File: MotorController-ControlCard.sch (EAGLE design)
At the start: 38 parts, among them J1 SL07-HORIZ, Q7 MOSFET-PCHANNEL, Q8 MOSFET-PCHANNEL, U1 TMS320F28069MPZT, U3 TMS320F28069MPZT

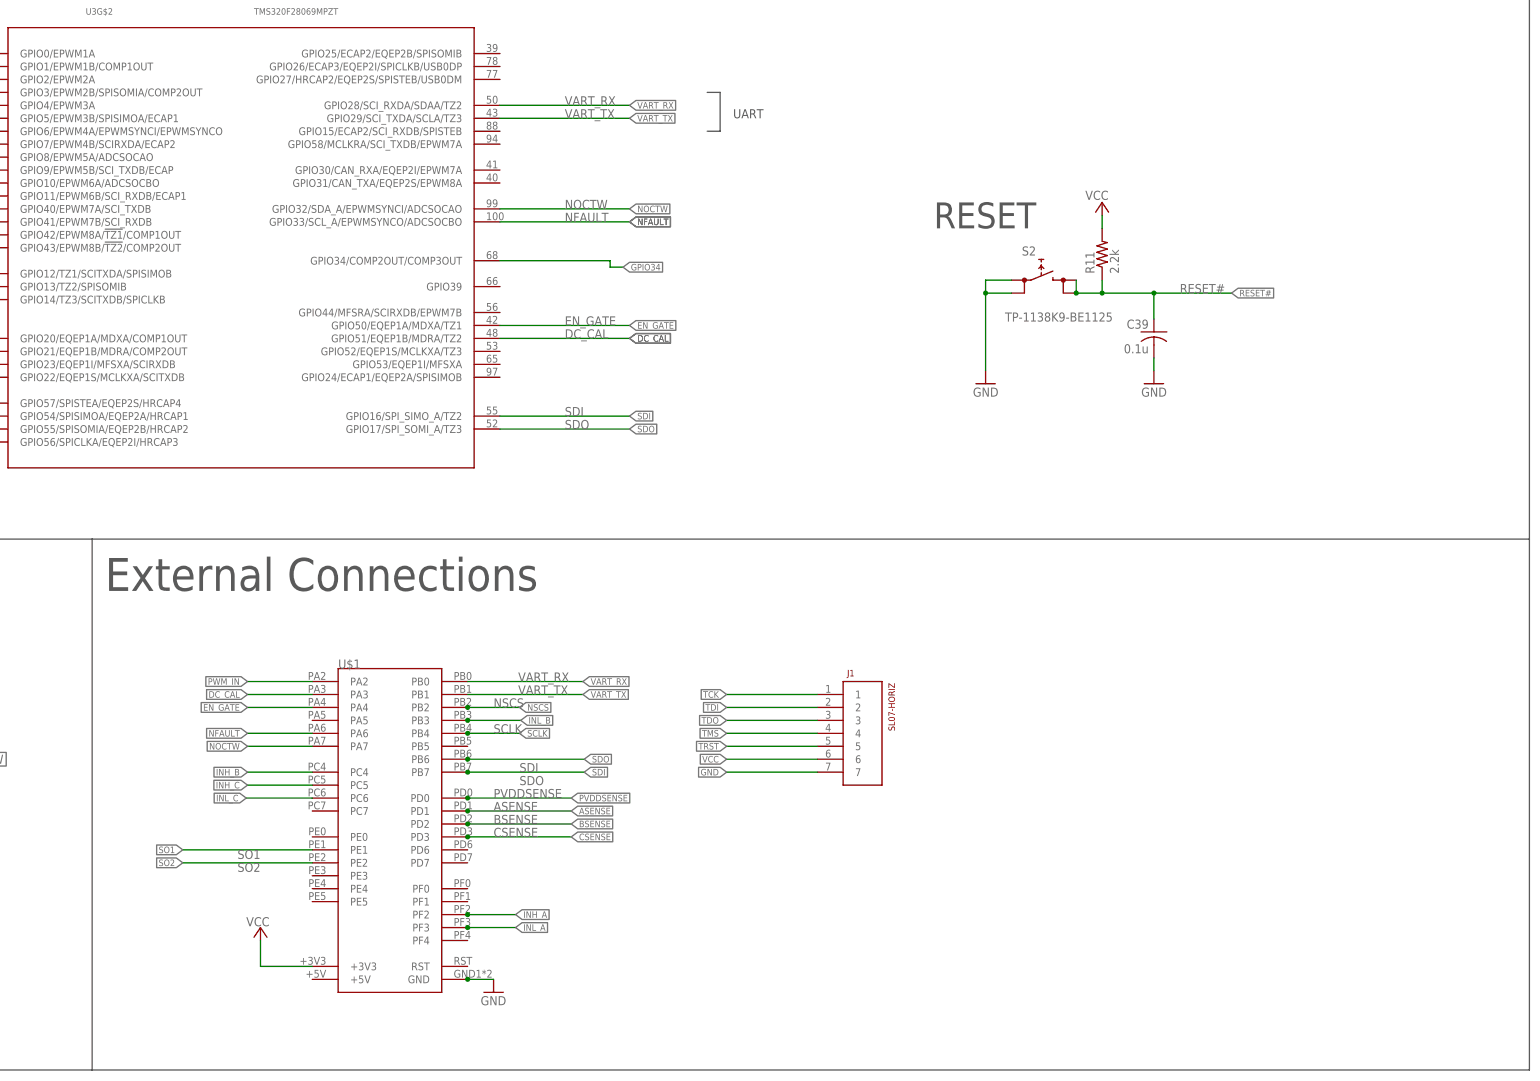
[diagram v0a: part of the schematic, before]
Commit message: Added SL connectors & MAX232, added Andrew's JTAG connector
Added SL connectors from gimbal power board and added connections to BOOSTXL header / MAX232. Same implementation as gimbal power board.
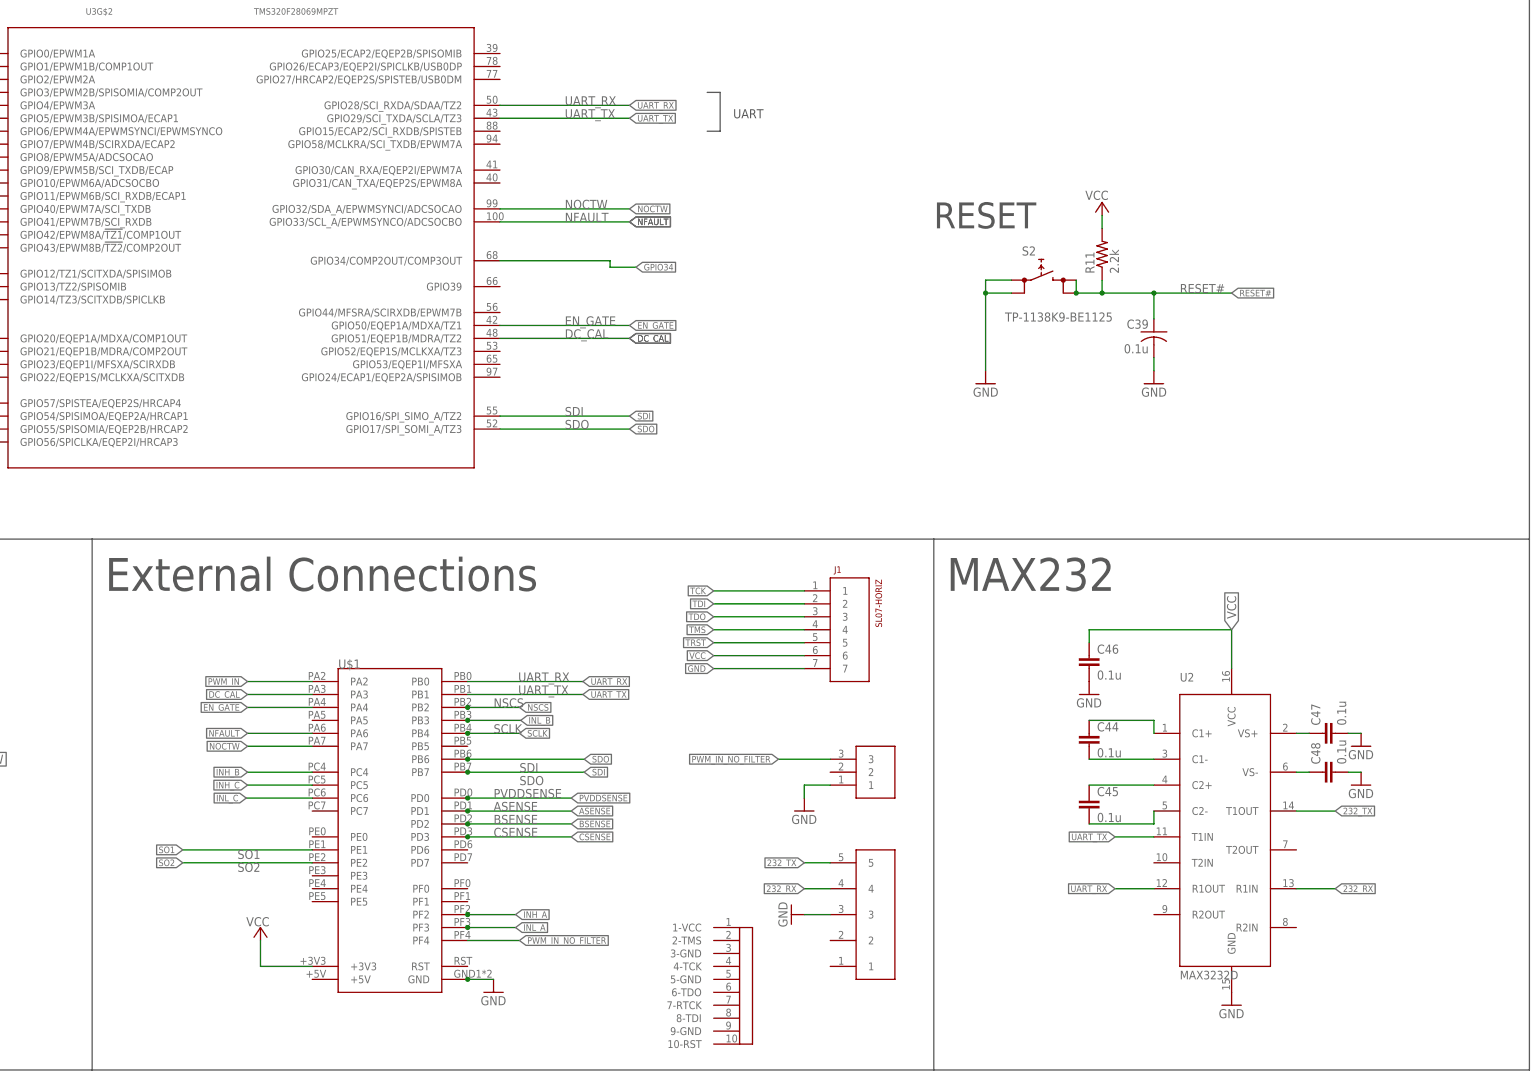
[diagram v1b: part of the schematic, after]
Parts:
- added C44, C45, C46, C47, C48: 0.1u, SparkFun-Passives:CAP0805
- added J2: SL03THROUGH_HOLE, MRDT-Connectors:SL03THROUGH_HOLE
- added U$2: IDC_BOX_HEADER_2X5_1.27MM, MRDT-Connectors:IDC_BOX_HEADER_2X5_1.27MM
- added U$4: 5PIN, Molex-SL:5PIN
- added U2: MAX3232D, MRDT-ICs:MAX3232D
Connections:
- removed net VART_RX: U$1.PB0, U3G$2.GPIO28/SCI_RXDA/SDAA/TZ2
- removed net VART_TX: U$1.PB1, U3G$2.GPIO29/SCI_TXDA/SCLA/TZ3
- new net 232_RX: U$4.4, U2.R1IN
- new net 232_TX: U$4.5, U2.T1OUT
- new net N$40: C44.1, U2.C1+
- new net N$42: C44.2, U2.C1-
- new net N$43: C45.1, U2.C2+
- new net N$44: C45.2, U2.C2-
- new net N$45: C48.1, U2.VS-
- new net N$46: C47.1, U2.VS+
- new net PWM_IN_NO_FILTER: J2.3, U$1.PF4
- new net UART_RX: U$1.PB0, U2.R1OUT, U3G$2.GPIO28/SCI_RXDA/SDAA/TZ2
- new net UART_TX: U$1.PB1, U2.T1IN, U3G$2.GPIO29/SCI_TXDA/SCLA/TZ3
- net GND: now also C46.2, C47.2, C48.2, J2.1, U$4.3, U2.GND
- net VCC: now also C46.1, U2.VCC
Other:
- note added: "MAX232"
- moved on the sheet: J1

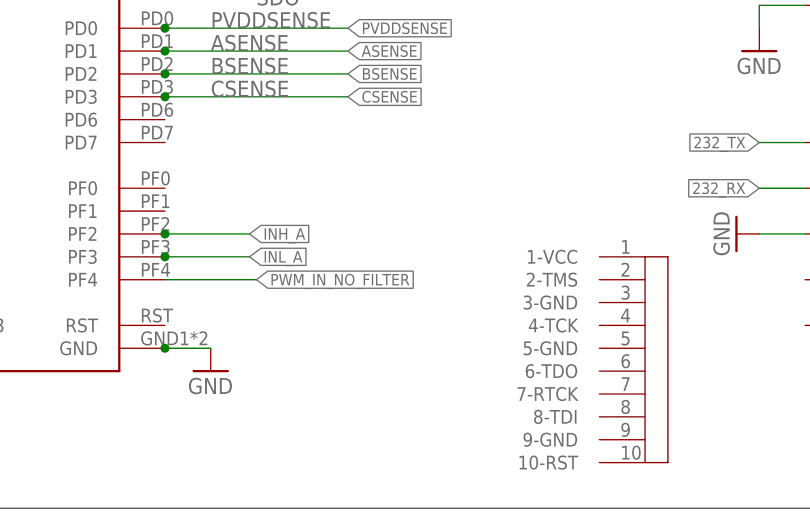
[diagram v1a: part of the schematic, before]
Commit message: Added connections to Andrew's JTAG connector
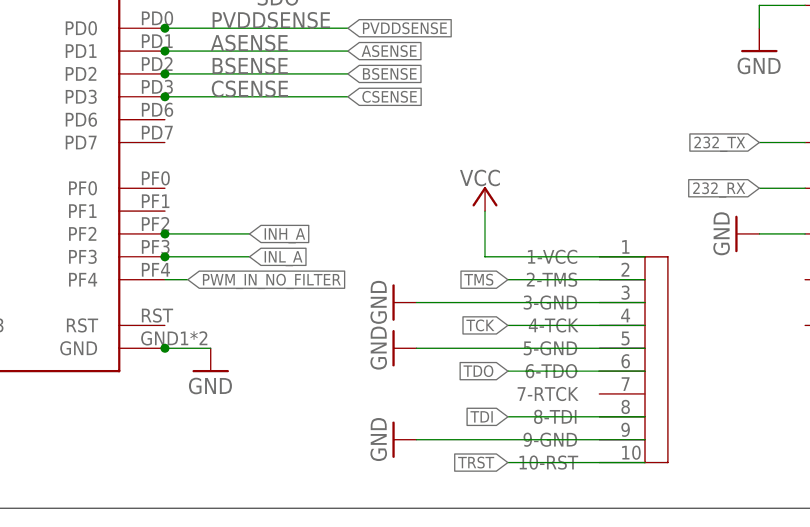
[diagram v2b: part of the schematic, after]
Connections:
- net +3V3: now also U$2.1-VCC
- net GND: now also U$2.3-GND, U$2.5-GND, U$2.9-GND
- net TCK: now also U$2.4-TCK
- net TDI: now also U$2.8-TDI
- net TDO: now also U$2.6-TDO
- net TMS: now also U$2.2-TMS
- net TRST: now also U$2.10-RST
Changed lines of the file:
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@@
 <part name="GND46" library="SparkFun-Aesthetics" deviceset="GND" device=""/>
 <part name="U$2" library="MRDT-Connectors" deviceset="IDC_BOX_HEADER_2X5_1.27MM" device=""/>
+<part name="VCC2" library="supply1" deviceset="+3V3" device="" value="VCC"/>
+<part name="GND2" library="SparkFun-Aesthetics" deviceset="GND" device=""/>
+<part name="GND3" library="SparkFun-Aesthetics" deviceset="GND" device=""/>
+<part name="GND4" library="SparkFun-Aesthetics" deviceset="GND" device=""/>
 </parts>
 <sheets>
@@
 <instance part="GND46" gate="1" x="251.46" y="-73.66"/>
 <instance part="U$2" gate="1" x="129.54" y="-124.46"/>
+<instance part="VCC2" gate="G$1" x="111.76" y="-93.98" smashed="yes">
+<attribute name="VALUE" x="108.966" y="-93.726" size="1.778" layer="96"/>
+</instance>
+<instance part="GND2" gate="1" x="101.6" y="-106.68" rot="R270"/>
+<instance part="GND3" gate="1" x="101.6" y="-111.76" rot="R270"/>
+<instance part="GND4" gate="1" x="101.6" y="-121.92" rot="R270"/>
 </instances>
 <busses>
@@
 <wire x1="251.46" y1="-71.12" x2="248.92" y2="-71.12" width="0.1524" layer="91"/>
 </segment>
+<segment>
+<pinref part="U$2" gate="1" pin="3-GND"/>
+<wire x1="129.54" y1="-106.68" x2="104.14" y2="-106.68" width="0.1524" layer="91"/>
+<pinref part="GND2" gate="1" pin="GND"/>
+</segment>
+<segment>
+<pinref part="U$2" gate="1" pin="5-GND"/>
+<wire x1="129.54" y1="-111.76" x2="104.14" y2="-111.76" width="0.1524" layer="91"/>
+<pinref part="GND3" gate="1" pin="GND"/>
+</segment>
+<segment>
+<pinref part="U$2" gate="1" pin="9-GND"/>
+<wire x1="129.54" y1="-121.92" x2="104.14" y2="-121.92" width="0.1524" layer="91"/>
+<pinref part="GND4" gate="1" pin="GND"/>
+</segment>
 </net>
 <net name="NOCTW" class="0">
@@
 <wire x1="35.56" y1="-109.22" x2="45.72" y2="-109.22" width="0.1524" layer="91"/>
 </segment>
+<segment>
+<pinref part="VCC2" gate="G$1" pin="+3V3"/>
+<wire x1="111.76" y1="-96.52" x2="111.76" y2="-101.6" width="0.1524" layer="91"/>
+<pinref part="U$2" gate="1" pin="1-VCC"/>
+<wire x1="111.76" y1="-101.6" x2="129.54" y2="-101.6" width="0.1524" layer="91"/>
+</segment>
 </net>
 <net name="TCK" class="0">
@@
 <label x="124.46" y="-35.56" size="1.27" layer="95" rot="R180" xref="yes"/>
 </segment>
+<segment>
+<pinref part="U$2" gate="1" pin="4-TCK"/>
+<wire x1="129.54" y1="-109.22" x2="114.3" y2="-109.22" width="0.1524" layer="91"/>
+<label x="114.3" y="-109.22" size="1.27" layer="95" rot="R180" xref="yes"/>
+</segment>
 </net>
 <net name="TDI" class="0">
@@
 <wire x1="142.24" y1="-38.1" x2="124.46" y2="-38.1" width="0.1524" layer="91"/>
 <label x="124.46" y="-38.1" size="1.27" layer="95" rot="R180" xref="yes"/>
+</segment>
+<segment>
+<pinref part="U$2" gate="1" pin="8-TDI"/>
+<wire x1="129.54" y1="-119.38" x2="114.3" y2="-119.38" width="0.1524" layer="91"/>
+<label x="114.3" y="-119.38" size="1.27" layer="95" rot="R180" xref="yes"/>
 </segment>
 </net>
@@
 <pinref part="U1" gate="G$1" pin="TDO/GPIO37"/>
 </segment>
+<segment>
+<pinref part="U$2" gate="1" pin="6-TDO"/>
+<wire x1="129.54" y1="-114.3" x2="114.3" y2="-114.3" width="0.1524" layer="91"/>
+<label x="114.3" y="-114.3" size="1.27" layer="95" rot="R180" xref="yes"/>
+</segment>
 </net>
 <net name="TMS" class="0">
@@
 <wire x1="142.24" y1="-43.18" x2="124.46" y2="-43.18" width="0.1524" layer="91"/>
 <label x="124.46" y="-43.18" size="1.27" layer="95" rot="R180" xref="yes"/>
+</segment>
+<segment>
+<pinref part="U$2" gate="1" pin="2-TMS"/>
+<wire x1="129.54" y1="-104.14" x2="114.3" y2="-104.14" width="0.1524" layer="91"/>
+<label x="114.3" y="-104.14" size="1.27" layer="95" rot="R180" xref="yes"/>
 </segment>
 </net>
@@
 <pinref part="U1" gate="G$1" pin="!TRST"/>
 <wire x1="68.58" y1="129.54" x2="162.56" y2="129.54" width="0.1524" layer="91"/>
+</segment>
+<segment>
+<pinref part="U$2" gate="1" pin="10-RST"/>
+<wire x1="129.54" y1="-124.46" x2="114.3" y2="-124.46" width="0.1524" layer="91"/>
+<label x="114.3" y="-124.46" size="1.27" layer="95" rot="R180" xref="yes"/>
 </segment>
 </net>
@@
 <segment>
 <pinref part="U$1" gate="G$1" pin="PF4"/>
-<wire x1="76.2" y1="-104.14" x2="86.36" y2="-104.14" width="0.1524" layer="91"/>
-<label x="86.36" y="-104.14" size="1.27" layer="95" xref="yes"/>
-</segment>
-</net>
+<wire x1="76.2" y1="-104.14" x2="78.74" y2="-104.14" width="0.1524" layer="91"/>
+<label x="78.74" y="-104.14" size="1.27" layer="95" xref="yes"/>
+</segment>
+</net>
